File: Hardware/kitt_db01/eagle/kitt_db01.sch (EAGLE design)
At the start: 99 parts, among them U9.00 ADNS-3080, U9.01 MIC5205-3.3YM5TR, U9.02 SI1922EDH, X9.00 RESON

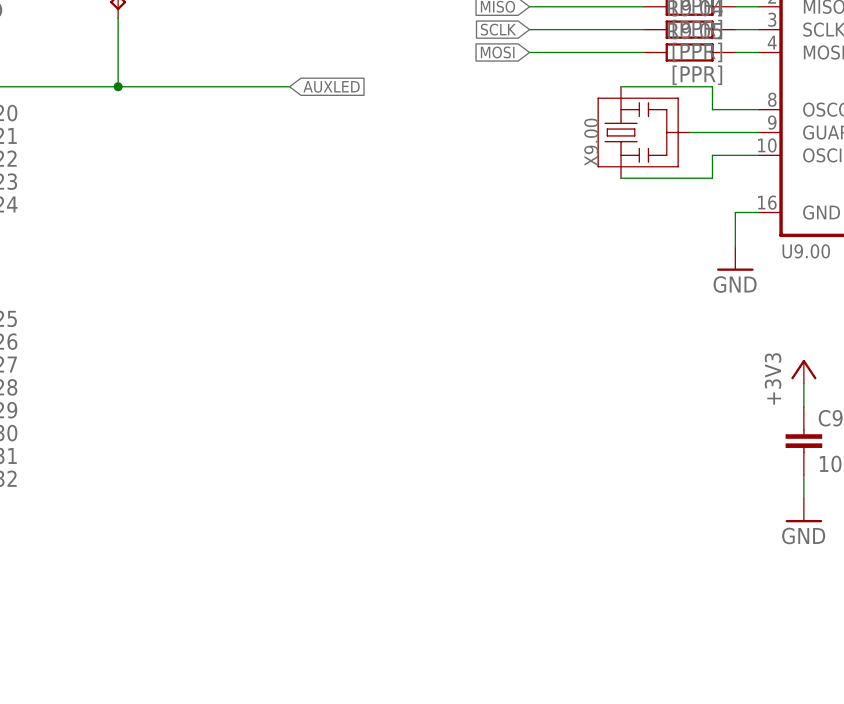
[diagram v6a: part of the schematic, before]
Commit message: updated bom; added pullups and a double I2C header
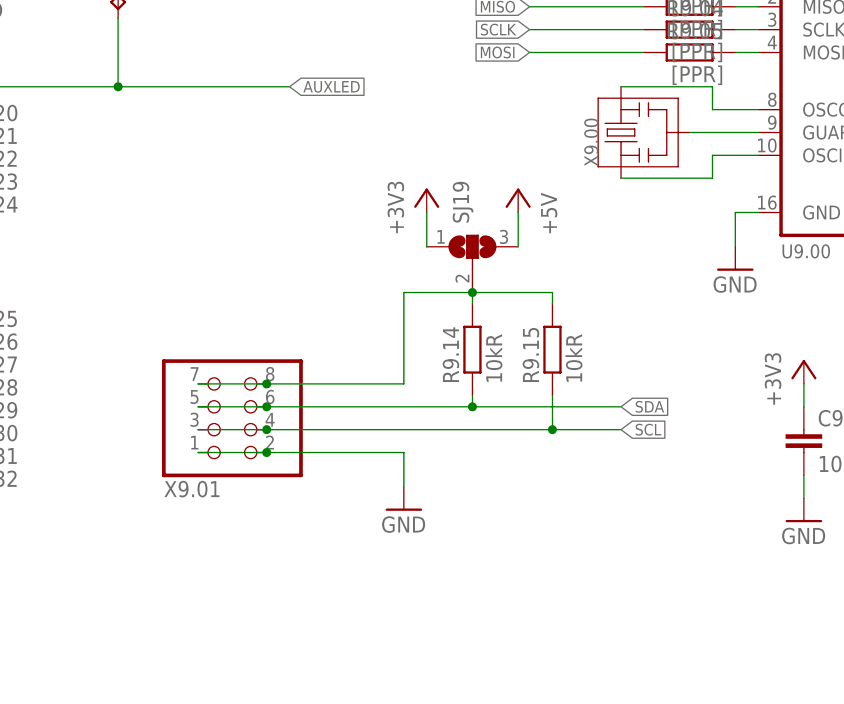
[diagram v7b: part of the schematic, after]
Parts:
- added R9.14, R9.15: 10kR, rcl:R-EU_R0805
- added SJ19: (no value), jumper:SJ2W
- added X9.01: (no value), pinhead:PINHD-2X4/90
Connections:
- new net N$44: R9.14.2, R9.15.2, SJ19.2, X9.01.7, X9.01.8
- net +3V3: now also SJ19.1
- net +5V: now also SJ19.3
- net GND: now also X9.01.1, X9.01.2
- net SCL: now also R9.15.1, X9.01.3, X9.01.4
- net SDA: now also R9.14.1, X9.01.5, X9.01.6
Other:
- note added: "TODO: Bus voltage selector and opt. pullups"
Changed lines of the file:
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@@
 <part name="R9.04" library="rcl" deviceset="R-EU_" device="R0805" value="[PPR]"/>
 <part name="R9.05" library="rcl" deviceset="R-EU_" device="R0805" value="[PPR]"/>
+<part name="X9.01" library="pinhead" deviceset="PINHD-2X4" device="/90"/>
+<part name="GND12" library="supply1" deviceset="GND" device=""/>
+<part name="R9.14" library="rcl" deviceset="R-EU_" device="R0805" value="10kR"/>
+<part name="R9.15" library="rcl" deviceset="R-EU_" device="R0805" value="10kR"/>
+<part name="SJ19" library="jumper" deviceset="SJ2W" device=""/>
+<part name="+3V10" library="supply1" deviceset="+3V3" device=""/>
+<part name="P+3" library="supply1" deviceset="+5V" device=""/>
 </parts>
 <sheets>
@@
 <text x="217.17" y="20.32" size="2.54" layer="94">D. Hoeglinger</text>
 <text x="162.56" y="17.78" size="1.27" layer="98">todo: clean up</text>
+<text x="48.26" y="59.69" size="1.27" layer="98">TODO: Bus voltage selector and opt. pullups</text>
 </plain>
 <instances>
@@
 <instance part="R9.04" gate="G$1" x="116.84" y="90.17" rot="MR0"/>
 <instance part="R9.05" gate="G$1" x="116.84" y="87.63" rot="MR0"/>
+<instance part="X9.01" gate="A" x="64.77" y="48.26" rot="MR180"/>
+<instance part="GND12" gate="1" x="85.09" y="36.83"/>
+<instance part="R9.14" gate="G$1" x="92.71" y="54.61" rot="R90"/>
+<instance part="R9.15" gate="G$1" x="101.6" y="54.61" rot="R90"/>
+<instance part="SJ19" gate="G$1" x="92.71" y="66.04" rot="R90"/>
+<instance part="+3V10" gate="G$1" x="87.63" y="72.39"/>
+<instance part="P+3" gate="1" x="97.79" y="72.39" rot="MR0"/>
 </instances>
 <busses>
@@
 <wire x1="243.84" y1="157.48" x2="243.84" y2="160.02" width="0.1524" layer="91"/>
 </segment>
+<segment>
+<pinref part="+3V10" gate="G$1" pin="+3V3"/>
+<pinref part="SJ19" gate="G$1" pin="1"/>
+<wire x1="87.63" y1="69.85" x2="87.63" y2="66.04" width="0.1524" layer="91"/>
+</segment>
 </net>
 <net name="GND" class="0">
@@
 <wire x1="247.65" y1="66.04" x2="247.65" y2="82.55" width="0.1524" layer="91"/>
 </segment>
+<segment>
+<pinref part="X9.01" gate="A" pin="1"/>
+<pinref part="X9.01" gate="A" pin="2"/>
+<wire x1="62.23" y1="43.18" x2="69.85" y2="43.18" width="0.1524" layer="91"/>
+<wire x1="69.85" y1="43.18" x2="85.09" y2="43.18" width="0.1524" layer="91"/>
+<junction x="69.85" y="43.18"/>
+<pinref part="GND12" gate="1" pin="GND"/>
+<wire x1="85.09" y1="39.37" x2="85.09" y2="43.18" width="0.1524" layer="91"/>
+</segment>
 </net>
 <net name="MOSI" class="0">
@@
 <wire x1="99.06" y1="152.4" x2="99.06" y2="157.48" width="0.1524" layer="91"/>
 </segment>
+<segment>
+<pinref part="P+3" gate="1" pin="+5V"/>
+<pinref part="SJ19" gate="G$1" pin="3"/>
+<wire x1="97.79" y1="69.85" x2="97.79" y2="66.04" width="0.1524" layer="91"/>
+</segment>
 </net>
 <net name="N$9" class="0">
@@
 <junction x="48.26" y="124.46"/>
 </segment>
+<segment>
+<pinref part="X9.01" gate="A" pin="3"/>
+<pinref part="X9.01" gate="A" pin="4"/>
+<wire x1="62.23" y1="45.72" x2="69.85" y2="45.72" width="0.1524" layer="91"/>
+<wire x1="69.85" y1="45.72" x2="101.6" y2="45.72" width="0.1524" layer="91"/>
+<junction x="69.85" y="45.72"/>
+<label x="109.22" y="45.72" size="1.27" layer="95" xref="yes"/>
+<pinref part="R9.15" gate="G$1" pin="1"/>
+<wire x1="101.6" y1="45.72" x2="109.22" y2="45.72" width="0.1524" layer="91"/>
+<wire x1="101.6" y1="49.53" x2="101.6" y2="45.72" width="0.1524" layer="91"/>
+<junction x="101.6" y="45.72"/>
+</segment>
 </net>
 <net name="SDA" class="0">
@@
 <wire x1="45.72" y1="127" x2="45.72" y2="121.92" width="0.1524" layer="91"/>
 <junction x="45.72" y="121.92"/>
+</segment>
+<segment>
+<pinref part="X9.01" gate="A" pin="5"/>
+<pinref part="X9.01" gate="A" pin="6"/>
+<wire x1="62.23" y1="48.26" x2="69.85" y2="48.26" width="0.1524" layer="91"/>
+<wire x1="69.85" y1="48.26" x2="92.71" y2="48.26" width="0.1524" layer="91"/>
+<junction x="69.85" y="48.26"/>
+<label x="109.22" y="48.26" size="1.27" layer="95" xref="yes"/>
+<pinref part="R9.14" gate="G$1" pin="1"/>
+<wire x1="92.71" y1="48.26" x2="109.22" y2="48.26" width="0.1524" layer="91"/>
+<wire x1="92.71" y1="49.53" x2="92.71" y2="48.26" width="0.1524" layer="91"/>
+<junction x="92.71" y="48.26"/>
 </segment>
 </net>
@@
 </segment>
 </net>
+<net name="N$44" class="0">
+<segment>
+<pinref part="X9.01" gate="A" pin="7"/>
+<pinref part="X9.01" gate="A" pin="8"/>
+<wire x1="62.23" y1="50.8" x2="69.85" y2="50.8" width="0.1524" layer="91"/>
+<wire x1="69.85" y1="50.8" x2="85.09" y2="50.8" width="0.1524" layer="91"/>
+<junction x="69.85" y="50.8"/>
+<pinref part="R9.14" gate="G$1" pin="2"/>
+<wire x1="85.09" y1="60.96" x2="85.09" y2="50.8" width="0.1524" layer="91"/>
+<wire x1="92.71" y1="59.69" x2="92.71" y2="60.96" width="0.1524" layer="91"/>
+<wire x1="92.71" y1="60.96" x2="85.09" y2="60.96" width="0.1524" layer="91"/>
+<pinref part="R9.15" gate="G$1" pin="2"/>
+<wire x1="92.71" y1="60.96" x2="101.6" y2="60.96" width="0.1524" layer="91"/>
+<wire x1="101.6" y1="60.96" x2="101.6" y2="59.69" width="0.1524" layer="91"/>
+<junction x="92.71" y="60.96"/>
+<pinref part="SJ19" gate="G$1" pin="2"/>
+</segment>
+</net>

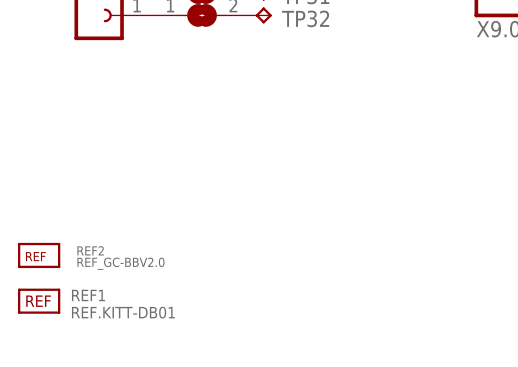
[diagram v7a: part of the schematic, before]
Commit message: snapshot of db01 board layout -> placement of top and bottom silkscreen acceptable -> todo: flip solderbridges on patching areas to bottom,    and also flip pin text to top
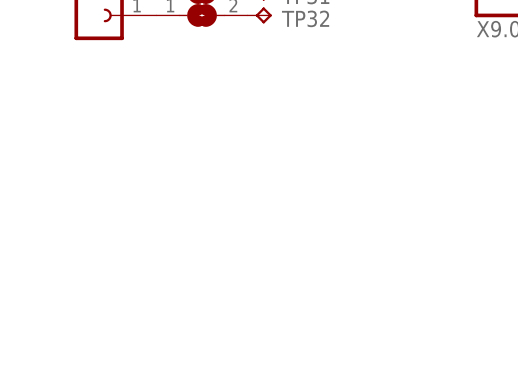
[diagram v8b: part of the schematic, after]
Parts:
- removed REF1: REF.KITT-DB01, kitt.refs:REF.KITT-DB01
- removed REF2: REF_GC-BBV2.0, kitt.con:REF_GC-BBV2.0
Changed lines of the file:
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@@
 <setting verticaltext="up"/>
 </settings>
-<grid distance="0.05" unitdist="inch" unit="inch" style="lines" multiple="1" display="no" altdistance="0.01" altunitdist="inch" altunit="inch"/>
+<grid distance="0.1" unitdist="inch" unit="inch" style="lines" multiple="1" display="no" altdistance="0.01" altunitdist="inch" altunit="inch"/>
 <layers>
 <layer number="1" name="Top" color="4" fill="1" visible="no" active="no"/>
@@
 <part name="D9.00" library="led" deviceset="LED" device="CHIP-LED0805" value="RED"/>
 <part name="R9.07" library="rcl" deviceset="R-EU_" device="R0805" value="[0R]"/>
-<part name="REF1" library="kitt.refs" deviceset="REF.KITT-DB01" device=""/>
-<part name="REF2" library="kitt.con" deviceset="REF_GC-BBV2.0" device=""/>
 <part name="SV1" library="con-lsta" deviceset="FE10-1" device=""/>
 <part name="GND7" library="supply1" deviceset="GND" device=""/>
@@
 <instance part="D9.00" gate="G$1" x="243.84" y="154.94"/>
 <instance part="R9.07" gate="G$1" x="187.96" y="76.2" rot="MR180"/>
-<instance part="REF1" gate="G$1" x="7.62" y="7.62"/>
-<instance part="REF2" gate="G$1" x="7.62" y="12.7"/>
 <instance part="SV1" gate="G$1" x="15.24" y="114.3" rot="MR180"/>
 <instance part="GND7" gate="1" x="38.1" y="93.98"/>
